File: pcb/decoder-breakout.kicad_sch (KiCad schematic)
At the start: 1 part, among them U1 LS7866-S

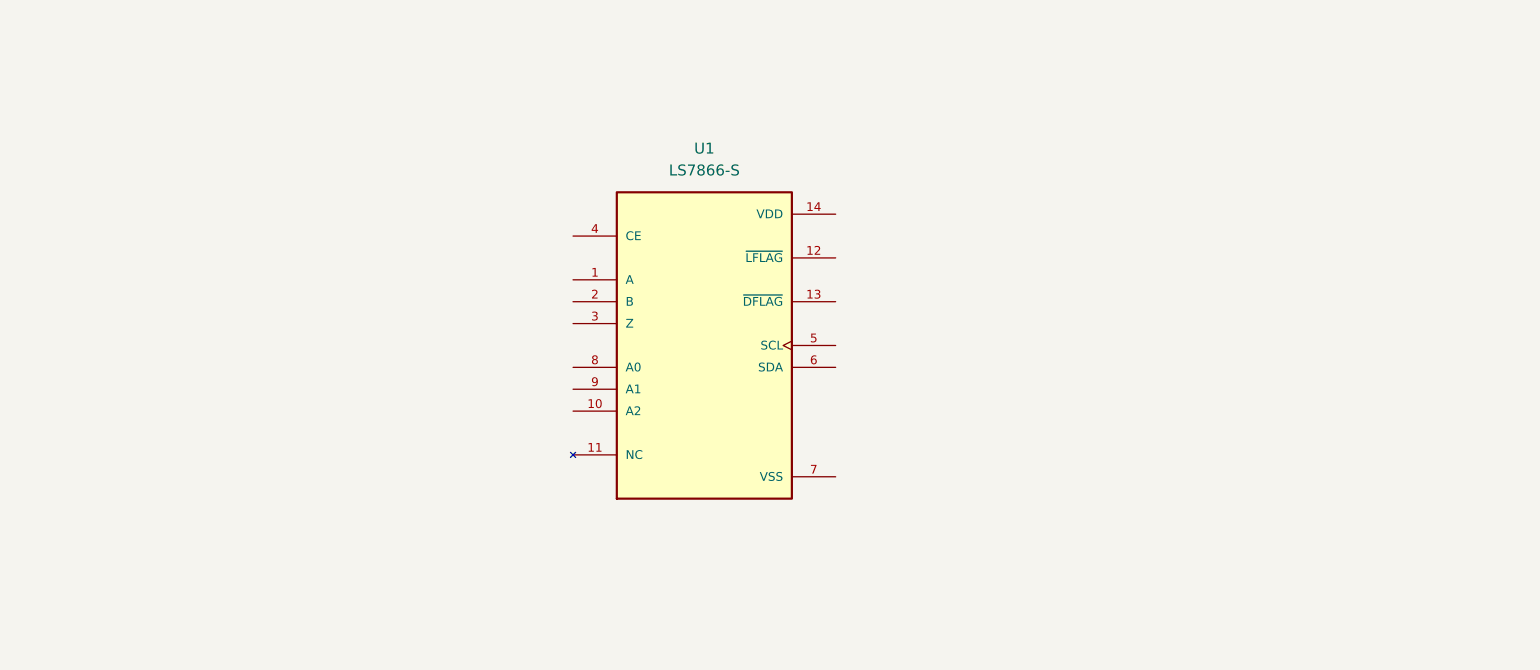
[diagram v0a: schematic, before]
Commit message: add resistors and jumpers
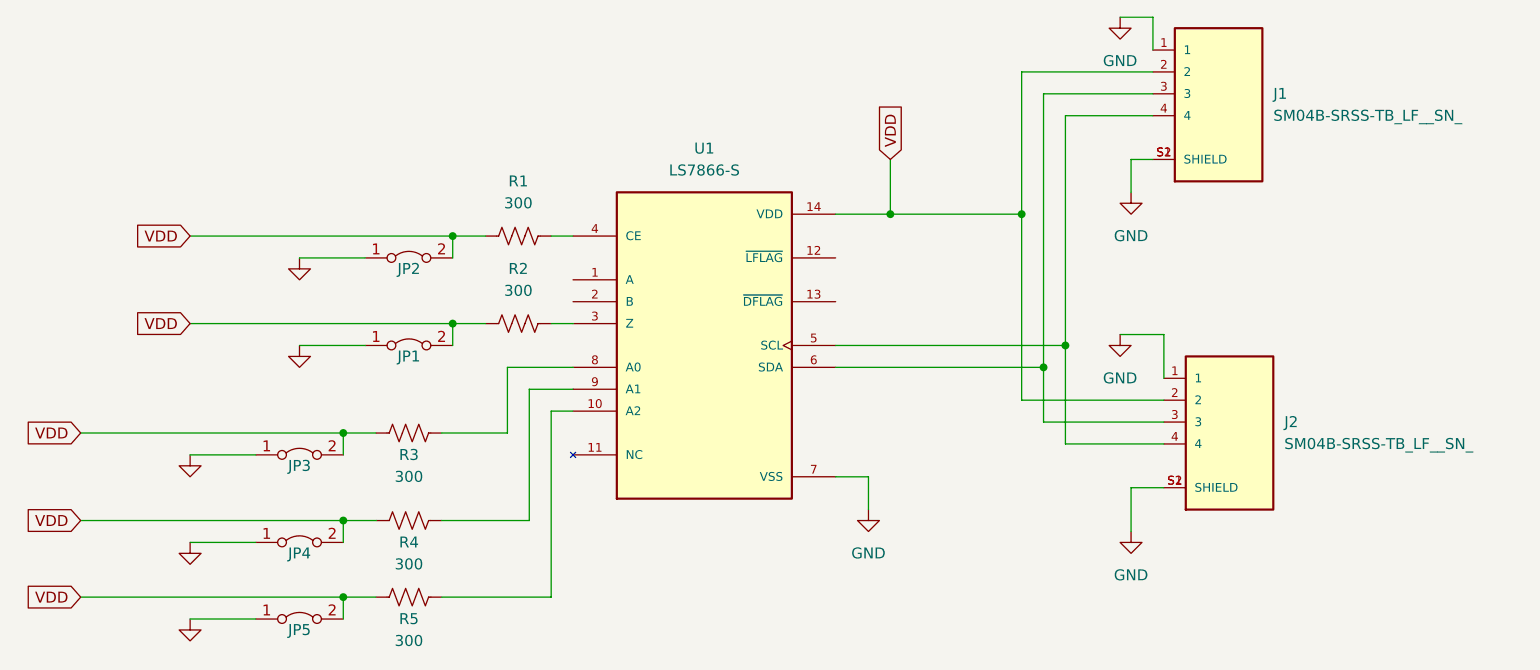
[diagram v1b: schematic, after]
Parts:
- added J1, J2: SM04B-SRSS-TB_LF__SN_, SM04B-SRSS-TB(LF)(SN):JST_SM04B-SRSS-TB_LF__SN_, symbol SM04B-SRSS-TB_LF__SN_:SM04B-SRSS-TB_LF__SN_
- added JP1, JP2, JP3, JP4, JP5: Jumper_2_Bridged, Connector_PinHeader_2.54mm:PinHeader_1x02_P2.54mm_Vertical, symbol Jumper:Jumper_2_Bridged
- added R1, R2, R3, R4, R5: 300, Resistor_SMD:R_2010_5025Metric_Pad1.40x2.65mm_HandSolder, symbol Device:R_US
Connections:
- net at U1.10 (A2): now also R5.1
- net VDD: now reaches U1.14 (VDD)
- net VDD: now also J1.2, J2.2, JP1.2 (B), JP2.2 (B), JP3.2 (B), JP4.2 (B), JP5.2 (B), R1.2, R2.2, R3.2, R4.2, R5.2
- net at U1.3 (Z): now also R2.1
- net at U1.4 (CE): now also R1.1
- net at U1.5 (SCL): now also J1.4, J2.4
- net at U1.6 (SDA): now also J1.3, J2.3
- net GND: now reaches U1.7 (VSS)
- net GND: now also J1.1, J1.S1 (SHIELD), J1.S2 (SHIELD), J2.1, J2.S1 (SHIELD), J2.S2 (SHIELD), JP1.1 (A), JP2.1 (A), JP3.1 (A), JP4.1 (A), JP5.1 (A)
- net at U1.8 (A0): now also R3.1
- net at U1.9 (A1): now also R4.1

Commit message: added jumpers for changing address, level shifters 3.3v->5v for encoders
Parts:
- removed JP1, JP2: Jumper_2_Bridged, Connector_PinHeader_2.54mm:PinHeader_1x02_P2.54mm_Vertical, symbol Jumper:Jumper_2_Bridged
- added Q1, Q2: BSS138, Package_TO_SOT_SMD:SOT-23, symbol Transistor_FET:BSS138
- added R6, R7, R8, R9: 10k, Resistor_SMD:R_2010_5025Metric_Pad1.40x2.65mm_HandSolder, symbol Device:R_US
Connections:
- net A: now reaches U1.1 (A)
- net A: now also Q1.1 (G), R6.1
- net B: now reaches U1.2 (B)
- net B: now also Q2.1 (G), R8.1
- new net: Q2.2 (S), R8.2
- new net: Q2.3 (D), R9.2
- new net: Q1.2 (S), R6.2
- new net: Q1.3 (D), R7.2
- new net +5v: R7.1, R9.1
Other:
- note added: "VDD is 3.3v"
- moved on the sheet: R1, R2

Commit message: added terminal block, started on PCB
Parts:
- added J3: TBL009-254-08GY-2GY, TBL009-254-08GY-2GY:CUI_TBL009-254-08GY-2GY, symbol TBL009-254-08GY-2GY:TBL009-254-08GY-2GY
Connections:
- net +5v: now also J3.1_A (1), J3.1_B (1__1), J3.6_A (6), J3.6_B (6__1)
- net A: now also Q1.2 (S), R6.2; no longer Q1.1 (G), R6.1
- net B: now also Q2.2 (S), R8.2; no longer Q2.1 (G), R8.1
- net GND: now also J3.2_A (2), J3.2_B (2__1), J3.5_A (5), J3.5_B (5__1)
- net VDD: now also Q1.1 (G), Q2.1 (G), R6.1, R8.1
- net Encoder_B: now reaches Q2.3 (D), R9.2
- net Encoder_B: now also J3.8_A (8), J3.8_B (8__1)
- net Encoder_A: now reaches Q1.3 (D), R7.2
- net Encoder_A: now also J3.7_A (7), J3.7_B (7__1)
- new net Shield: J3.3_A (3), J3.3_B (3__1), J3.4_A (4), J3.4_B (4__1)
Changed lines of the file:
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@@
     (effects (font (size 1.27 1.27)) (justify left bottom))
   )
+  (global_label "GND" (shape input) (at 264.16 120.65 180) (fields_autoplaced)
+    (effects (font (size 1.27 1.27)) (justify right))
+    (property "Intersheetrefs" "${INTERSHEET_REFS}" (at 257.3043 120.65 0)
+      (effects (font (size 1.27 1.27)) (justify right) hide)
+    )
+  )
+  (global_label "GND" (shape input) (at 264.16 138.43 180) (fields_autoplaced)
+    (effects (font (size 1.27 1.27)) (justify right))
+    (property "Intersheetrefs" "${INTERSHEET_REFS}" (at 257.3043 138.43 0)
+      (effects (font (size 1.27 1.27)) (justify right) hide)
+    )
+  )
   (global_label "VDD" (shape input) (at 86.36 78.74 180) (fields_autoplaced)
     (effects (font (size 1.27 1.27)) (justify right))
@@
     )
   )
+  (global_label "Encoder_A" (shape input) (at 147.32 171.45 0) (fields_autoplaced)
+    (effects (font (size 1.27 1.27)) (justify left))
+    (property "Intersheetrefs" "${INTERSHEET_REFS}" (at 159.9208 171.45 0)
+      (effects (font (size 1.27 1.27)) (justify left) hide)
+    )
+  )
+  (global_label "+5v" (shape input) (at 264.16 115.57 180) (fields_autoplaced)
+    (effects (font (size 1.27 1.27)) (justify right))
+    (property "Intersheetrefs" "${INTERSHEET_REFS}" (at 257.4253 115.57 0)
+      (effects (font (size 1.27 1.27)) (justify right) hide)
+    )
+  )
   (global_label "+5v" (shape input) (at 199.39 132.08 90) (fields_autoplaced)
     (effects (font (size 1.27 1.27)) (justify left))
@@
     )
   )
+  (global_label "GND" (shape input) (at 195.58 110.49 180) (fields_autoplaced)
+    (effects (font (size 1.27 1.27)) (justify right))
+    (property "Intersheetrefs" "${INTERSHEET_REFS}" (at 188.7243 110.49 0)
+      (effects (font (size 1.27 1.27)) (justify right) hide)
+    )
+  )
+  (global_label "VDD" (shape input) (at 172.72 129.54 90) (fields_autoplaced)
+    (effects (font (size 1.27 1.27)) (justify left))
+    (property "Intersheetrefs" "${INTERSHEET_REFS}" (at 172.72 122.9262 90)
+      (effects (font (size 1.27 1.27)) (justify left) hide)
+    )
+  )
   (global_label "VDD" (shape input) (at 86.36 88.9 180) (fields_autoplaced)
     (effects (font (size 1.27 1.27)) (justify right))
@@
     )
   )
+  (global_label "+5v" (shape input) (at 264.16 143.51 180) (fields_autoplaced)
+    (effects (font (size 1.27 1.27)) (justify right))
+    (property "Intersheetrefs" "${INTERSHEET_REFS}" (at 257.4253 143.51 0)
+      (effects (font (size 1.27 1.27)) (justify right) hide)
+    )
+  )
   (global_label "VDD" (shape input) (at 73.66 101.6 180) (fields_autoplaced)
     (effects (font (size 1.27 1.27)) (justify right))
@@
     )
   )
+  (global_label "A" (shape input) (at 105.41 171.45 180) (fields_autoplaced)
+    (effects (font (size 1.27 1.27)) (justify right))
+    (property "Intersheetrefs" "${INTERSHEET_REFS}" (at 101.3362 171.45 0)
+      (effects (font (size 1.27 1.27)) (justify right) hide)
+    )
+  )
   (global_label "VDD" (shape input) (at 167.64 69.85 90) (fields_autoplaced)
     (effects (font (size 1.27 1.27)) (justify left))
@@
     )
   )
+  (global_label "Encoder_B" (shape input) (at 264.16 151.13 180) (fields_autoplaced)
+    (effects (font (size 1.27 1.27)) (justify right))
+    (property "Intersheetrefs" "${INTERSHEET_REFS}" (at 251.3778 151.13 0)
+      (effects (font (size 1.27 1.27)) (justify right) hide)
+    )
+  )
+  (global_label "B" (shape input) (at 165.1 157.48 180) (fields_autoplaced)
+    (effects (font (size 1.27 1.27)) (justify right))
+    (property "Intersheetrefs" "${INTERSHEET_REFS}" (at 160.8448 157.48 0)
+      (effects (font (size 1.27 1.27)) (justify right) hide)
+    )
+  )
+  (global_label "Shield" (shape input) (at 264.16 130.81 180) (fields_autoplaced)
+    (effects (font (size 1.27 1.27)) (justify right))
+    (property "Intersheetrefs" "${INTERSHEET_REFS}" (at 255.3087 130.81 0)
+      (effects (font (size 1.27 1.27)) (justify right) hide)
+    )
+  )
   (global_label "B" (shape input) (at 130.81 86.36 180) (fields_autoplaced)
     (effects (font (size 1.27 1.27)) (justify right))
@@
     )
   )
-  (global_label "A" (shape input) (at 113.03 143.51 90) (fields_autoplaced)
-    (effects (font (size 1.27 1.27)) (justify left))
-    (property "Intersheetrefs" "${INTERSHEET_REFS}" (at 113.03 139.4362 90)
-      (effects (font (size 1.27 1.27)) (justify left) hide)
+  (global_label "Encoder_B" (shape input) (at 207.01 157.48 0) (fields_autoplaced)
+    (effects (font (size 1.27 1.27)) (justify left))
+    (property "Intersheetrefs" "${INTERSHEET_REFS}" (at 219.7922 157.48 0)
+      (effects (font (size 1.27 1.27)) (justify left) hide)
+    )
+  )
+  (global_label "GND" (shape input) (at 264.16 123.19 180) (fields_autoplaced)
+    (effects (font (size 1.27 1.27)) (justify right))
+    (property "Intersheetrefs" "${INTERSHEET_REFS}" (at 257.3043 123.19 0)
+      (effects (font (size 1.27 1.27)) (justify right) hide)
+    )
+  )
+  (global_label "Shield" (shape input) (at 264.16 128.27 180) (fields_autoplaced)
+    (effects (font (size 1.27 1.27)) (justify right))
+    (property "Intersheetrefs" "${INTERSHEET_REFS}" (at 255.3087 128.27 0)
+      (effects (font (size 1.27 1.27)) (justify right) hide)
+    )
+  )
+  (global_label "VDD" (shape input) (at 113.03 143.51 90) (fields_autoplaced)
+    (effects (font (size 1.27 1.27)) (justify left))
+    (property "Intersheetrefs" "${INTERSHEET_REFS}" (at 113.03 136.8962 90)
+      (effects (font (size 1.27 1.27)) (justify left) hide)
+    )
+  )
+  (global_label "+5v" (shape input) (at 264.16 140.97 180) (fields_autoplaced)
+    (effects (font (size 1.27 1.27)) (justify right))
+    (property "Intersheetrefs" "${INTERSHEET_REFS}" (at 257.4253 140.97 0)
+      (effects (font (size 1.27 1.27)) (justify right) hide)
+    )
+  )
+  (global_label "Encoder_A" (shape input) (at 264.16 148.59 180) (fields_autoplaced)
+    (effects (font (size 1.27 1.27)) (justify right))
+    (property "Intersheetrefs" "${INTERSHEET_REFS}" (at 251.5592 148.59 0)
+      (effects (font (size 1.27 1.27)) (justify right) hide)
+    )
+  )
+  (global_label "Shield" (shape input) (at 264.16 125.73 180) (fields_autoplaced)
+    (effects (font (size 1.27 1.27)) (justify right))
+    (property "Intersheetrefs" "${INTERSHEET_REFS}" (at 255.3087 125.73 0)
+      (effects (font (size 1.27 1.27)) (justify right) hide)
     )
   )
@@
     )
   )
-  (global_label "B" (shape input) (at 172.72 129.54 90) (fields_autoplaced)
-    (effects (font (size 1.27 1.27)) (justify left))
-    (property "Intersheetrefs" "${INTERSHEET_REFS}" (at 172.72 125.2848 90)
-      (effects (font (size 1.27 1.27)) (justify left) hide)
+  (global_label "GND" (shape input) (at 264.16 135.89 180) (fields_autoplaced)
+    (effects (font (size 1.27 1.27)) (justify right))
+    (property "Intersheetrefs" "${INTERSHEET_REFS}" (at 257.3043 135.89 0)
+      (effects (font (size 1.27 1.27)) (justify right) hide)
+    )
+  )
+  (global_label "Encoder_A" (shape input) (at 264.16 146.05 180) (fields_autoplaced)
+    (effects (font (size 1.27 1.27)) (justify right))
+    (property "Intersheetrefs" "${INTERSHEET_REFS}" (at 251.5592 146.05 0)
+      (effects (font (size 1.27 1.27)) (justify right) hide)
     )
   )
@@
     (property "Intersheetrefs" "${INTERSHEET_REFS}" (at 139.7 139.3153 90)
       (effects (font (size 1.27 1.27)) (justify left) hide)
+    )
+  )
+  (global_label "Encoder_B" (shape input) (at 264.16 153.67 180) (fields_autoplaced)
+    (effects (font (size 1.27 1.27)) (justify right))
+    (property "Intersheetrefs" "${INTERSHEET_REFS}" (at 251.3778 153.67 0)
+      (effects (font (size 1.27 1.27)) (justify right) hide)
+    )
+  )
+  (global_label "Shield" (shape input) (at 264.16 133.35 180) (fields_autoplaced)
+    (effects (font (size 1.27 1.27)) (justify right))
+    (property "Intersheetrefs" "${INTERSHEET_REFS}" (at 255.3087 133.35 0)
+      (effects (font (size 1.27 1.27)) (justify right) hide)
+    )
+  )
+  (global_label "+5v" (shape input) (at 264.16 118.11 180) (fields_autoplaced)
+    (effects (font (size 1.27 1.27)) (justify right))
+    (property "Intersheetrefs" "${INTERSHEET_REFS}" (at 257.4253 118.11 0)
+      (effects (font (size 1.27 1.27)) (justify right) hide)
     )
   )
@@
         )
       )
+    )
+  )
+  (symbol (lib_id "TBL009-254-08GY-2GY:TBL009-254-08GY-2GY") (at 274.32 125.73 0) (unit 1)
+    (in_bom yes) (on_board yes) (dnp no) (fields_autoplaced)
+    (property "Reference" "J3" (at 280.67 133.35 0)
+      (effects (font (size 1.27 1.27)) (justify left))
+    )
+    (property "Value" "TBL009-254-08GY-2GY" (at 280.67 135.89 0)
+      (effects (font (size 1.27 1.27)) (justify left))
+    )
+    (property "Footprint" "TBL009-254-08GY-2GY:CUI_TBL009-254-08GY-2GY" (at 274.32 125.73 0)
+      (effects (font (size 1.27 1.27)) (justify bottom) hide)
+    )
+    (property "Datasheet" "" (at 274.32 125.73 0)
+      (effects (font (size 1.27 1.27)) hide)
+    )
+    (property "MANUFACTURER" "CUI" (at 274.32 125.73 0)
+      (effects (font (size 1.27 1.27)) (justify bottom) hide)
+    )
+    (property "STANDARD" "Manufacturer Recommendations" (at 274.32 125.73 0)
+      (effects (font (size 1.27 1.27)) (justify bottom) hide)
+    )
+    (pin "7_A")
+    (pin "1_B")
+    (pin "4_A")
+    (pin "1_A")
+    (pin "6_A")
+    (pin "3_B")
+    (pin "8_B")
+    (pin "8_A")
+    (pin "5_B")
+    (pin "7_B")
+    (pin "2_A")
+    (pin "5_A")
+    (pin "2_B")
+    (pin "4_B")
+    (pin "6_B")
+    (pin "3_A")
+    (instances
+      (project "decoder-breakout"
+        (path "/1a0ebad1-ea8c-4043-8a0c-94ccddf3b0fc"
+          (reference "J3") (unit 1)
+        )
+      )
